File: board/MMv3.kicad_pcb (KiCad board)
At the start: 2 copper layers, 69 x 72 mm, 47 parts, among them J1 9V, J2 DRV8833_L, J3 left_mot, J4 right_mot, J5 DRV8833_R, Q1 DMG2301L, Q2 DMG2302U, Q3 DMG2302U, Q4 DMG2302U, SW1 PWR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

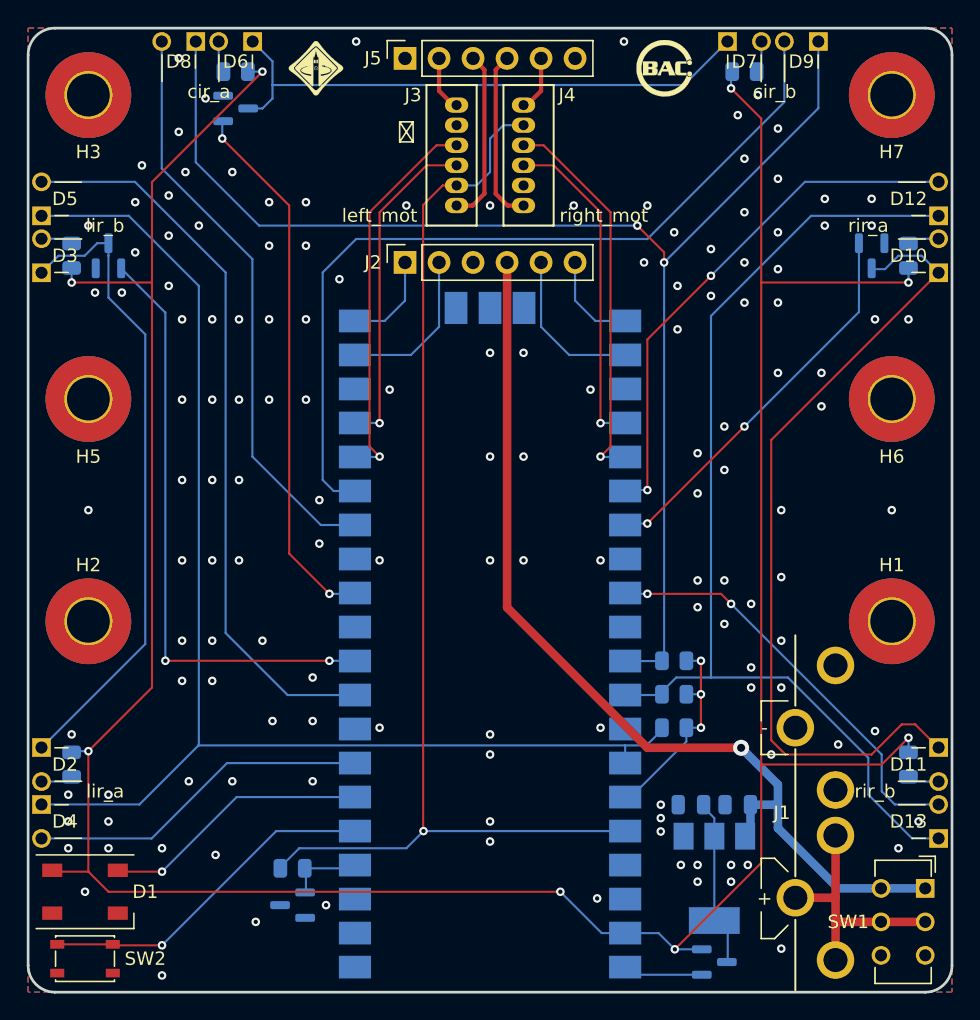
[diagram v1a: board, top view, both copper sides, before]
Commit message: Finished silkscreen and moving components
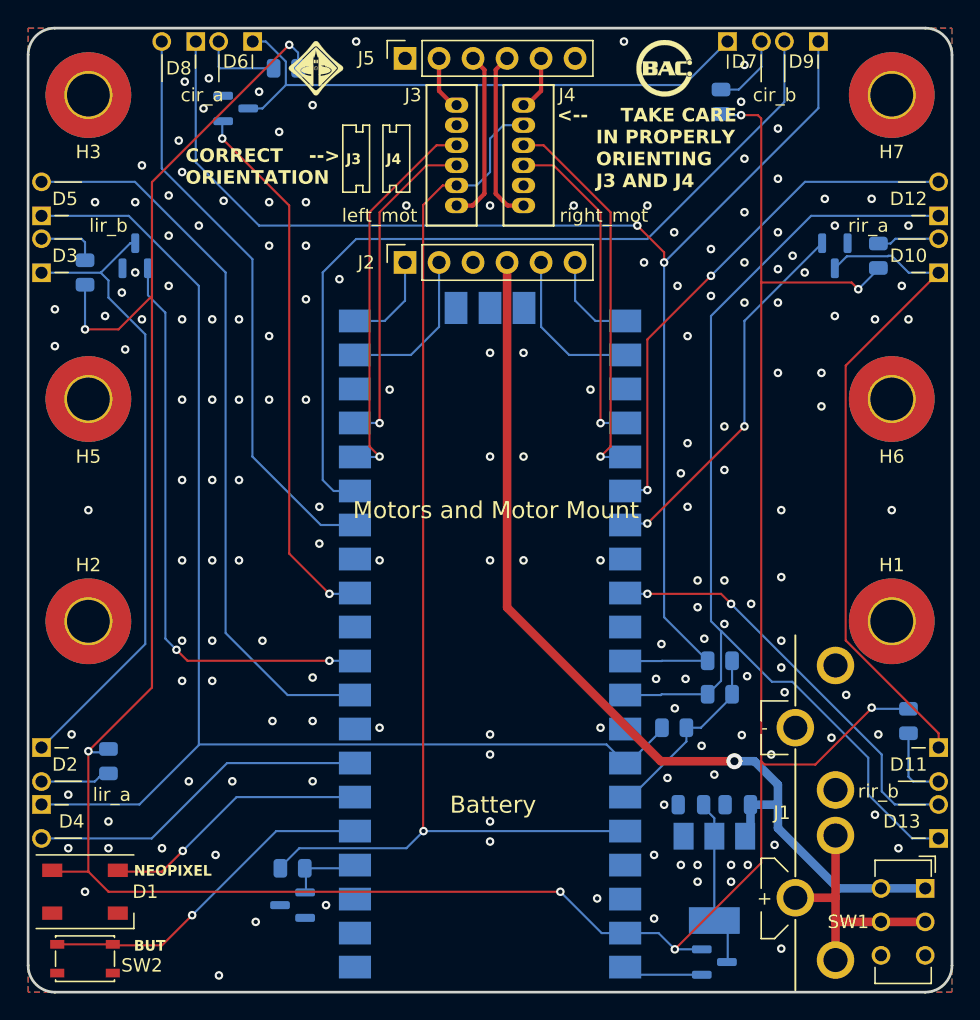
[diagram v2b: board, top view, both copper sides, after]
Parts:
- moved R7 3.76 mm to (134.8, 67.0)
- moved R2 3.41 mm to (167.2, 111.2)
- moved R3 3.41 mm to (167.2, 113.8)
- moved R10 3.25 mm to (181.2, 115.8)
- moved R8 2.85 mm to (167.2, 69.5), turned to 90 degrees
- moved R5 2.76 mm to (121.5, 118.8)
- moved Q4 2.75 mm to (175.8, 81.0)
- moved R9 2.25 mm to (179.0, 81.0)
- moved Q2 2.00 mm to (123.5, 81.0)
- moved R6 1.60 mm to (119.8, 82.2)
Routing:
- net Net-(D10-Pad1): track 60.6 -> 49.9 mm
- net /c_adc: track 101.4 -> 106.1 mm
- net +5V: track 219.7 -> 223.8 mm
- net Net-(D6-Pad2): track 2.40 -> 6.04 mm
- net Net-(D11-Pad2): track 2.40 -> 5.65 mm
- net Net-(D7-Pad2): track 2.40 -> 5.61 mm
- net Net-(D2-Pad2): track 2.40 -> 5.15 mm
- net Net-(D3-Pad2): track 2.40 -> 4.70 mm
- net Net-(D10-Pad2): track 2.40 -> 4.65 mm
- net /r_adc: track 77.8 -> 79.6 mm
- net /lir_en: track 44.8 -> 43.1 mm
- net /+3V3A: track 15.6 -> 14.4 mm, vias 3 -> 0
- net /rir_en: track 29.3 -> 28.0 mm
- net GND: track 0.00 -> 0.05 mm, vias 143 -> 165
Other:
- board text added: "3V3"
- board text added: "3V3A"
- board text added: "5V"
- board text added: "<-- TAKE CARE IN PROPERLY ORIENTING J3 AND J4"
- board text added: "BUT"
- board text added: "Battery"
- board text added: "CIR_A"
- board text added: "CIR_B"
- board text added: "CIR_EN"
- board text added: "CORRECT --> ORIENTATION"
- board text added: "C_ADC"
- board text added: "DO NOT PUT HEADERS ON THIS SIDE"
- board text added: "GND"
- board text added: "J3"
- board text added: "J4"
- board text added: "LENC_A"
- board text added: "LENC_B"
- board text added: "LIR_A"
- board text added: "LIR_B"
- board text added: "LIR_EN"
- board text added: "LMOT_IN1"
- board text added: "LMOT_IN2"
- board text added: "L_ADC"
- board text added: "MMv3.4 Orig: Matt Tran Rev: LJ Labata"
- board text added: "Motors and Motor Mount"
- board text added: "NEOPIXEL"
- board text added: "RENC_A"
- board text added: "RENC_B"
- board text added: "RIR_A"
- board text added: "RIR_B"
- board text added: "RIR_EN"
- board text added: "RMOT_IN1"
- board text added: "RMOT_IN2"
- board text added: "R_ADC"
- board text added: "VBUS"
- board text added: "lenc_a"
- board text added: "lenc_b"
- board text added: "lmot_in1"
- board text added: "lmot_in2"
- board text added: "lmot_m1"
- board text added: "lmot_m2"
- board text added: "renc_a"
- board text added: "renc_b"
- board text added: "rmot_in1"
- board text added: "rmot_in2"
- board text added: "rmot_m1"
- board text added: "rmot_m2"
- board text removed: "MMv3.3 Matt Tran"

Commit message: Changed silkscreen from 3.4 to 3.5
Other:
- board text added: "MMv3.5 Orig: Matt Tran Rev: LJ Labata"
- board text removed: "MMv3.4 Orig: Matt Tran Rev: LJ Labata"
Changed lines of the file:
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@@
 		)
 	)
-	(gr_text "MMv3.4\nOrig: Matt Tran\nRev: LJ Labata"
+	(gr_text "MMv3.5\nOrig: Matt Tran\nRev: LJ Labata"
 		(at 116.75 133 0)
 		(layer "B.SilkS")

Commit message: idk?
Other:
- board text added: "For J1 make sure the connectors are Level and Parallel! (Use a 9V Battery)"
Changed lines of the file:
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@@
+		(layer "F.SilkS")
+	)
+	(gr_rect
+		(start 159.4 69.4)
+		(end 170 76.4)
+		(stroke
+			(width 0.12)
+			(type default)
+		)
+		(fill none)
 		(layer "F.SilkS")
 	)
@@
 		(layer "F.SilkS")
 	)
+	(gr_rect
+		(start 127 72.4)
+		(end 137.2 76)
+		(stroke
+			(width 0.12)
+			(type default)
+		)
+		(fill none)
+		(layer "F.SilkS")
+	)
+	(gr_line
+		(start 170.8 122.4)
+		(end 169.8 122.4)
+		(stroke
+			(width 0.12)
+			(type default)
+		)
+		(layer "F.SilkS")
+	)
 	(gr_line
 		(start 143 71.25)
@@
 	)
 	(gr_line
+		(start 161.8 117.2)
+		(end 170.8 122.4)
+		(stroke
+			(width 0.12)
+			(type default)
+		)
+		(layer "F.SilkS")
+	)
+	(gr_line
 		(start 142.75 74.75)
 		(end 142.75 74.75)
@@
 	)
 	(gr_line
+		(start 160 116.2)
+		(end 160 118)
+		(stroke
+			(width 0.12)
+			(type default)
+		)
+		(layer "F.SilkS")
+	)
+	(gr_line
 		(start 172.25 118.25)
 		(end 170.25 118.25)
@@
 		(layer "F.SilkS")
 	)
+	(gr_rect
+		(start 154.6 112.8)
+		(end 161.8 128)
+		(stroke
+			(width 0.12)
+			(type default)
+		)
+		(fill none)
+		(layer "F.SilkS")
+	)
 	(gr_line
 		(start 140 75.75)
@@
 	)
 	(gr_line
+		(start 170.8 122.4)
+		(end 170.4 121.6)
+		(stroke
+			(width 0.12)
+			(type default)
+		)
+		(layer "F.SilkS")
+	)
+	(gr_line
 		(start 142 71.25)
 		(end 142.5 71.25)
@@
 			(width 0.12)
 			(type solid)
+		)
+		(layer "F.SilkS")
+	)
+	(gr_line
+		(start 169.8 122.4)
+		(end 170.4 121.6)
+		(stroke
+			(width 0.12)
+			(type default)
 		)
 		(layer "F.SilkS")
@@
 	)
 	(gr_text "Battery"
-		(at 147 122.75 0)
+		(at 138.2 122.6 0)
 		(layer "F.SilkS")
 		(effects
@@
 		)
 	)
+	(gr_text "For J1 make sure \nthe connectors are \nLevel and Parallel!\n(Use a 9V Battery)"
+		(at 155.2 113 -90)
+		(layer "F.SilkS")
+		(effects
+			(font
+				(size 1.016 1.016)
+				(thickness 0.1524)
+			)
+			(justify left bottom)
+		)
+	)
 	(gr_text "+"
 		(at 170.5 129 0)
@@
 	)
 	(gr_text "cir_b"
-		(at 171.25 69 0)
-		(layer "F.SilkS")
-		(effects
+		(at 172.2 69 0)
+		(layer "F.SilkS")
+		(effects

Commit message: finished mmv3_5 now bought
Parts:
- removed R1: 1k, Resistor_SMD:R_0805_2012Metric
- removed U1: DS28E05R+T, Package_TO_SOT_SMD:SOT-23
- SW2: footprint Button_Switch_SMD:SW_SPST_PTS810 -> 1825966_1 (1):SWDIP2_256X170P100
- moved SW2 6.73 mm to (116.7, 127.5), turned to 180 degrees
- moved D1 4.00 mm to (119.8, 132.5)
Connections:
- U3 pad 4: /onewire -> unconnected-(U3-GP2-Pad4)
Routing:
- net +3V3: track 85.2 -> 73.3 mm
- net /but: track 25.8 -> 18.2 mm, vias 1 -> 0
- net /onewire: track 5.68 -> 0.00 mm
- net +5V: track 223.8 -> 228.6 mm
- net /neopixel: track 20.1 -> 24.4 mm
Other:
- board text added: "9V"
- board text added: "x"
- board text removed: "1wire"
